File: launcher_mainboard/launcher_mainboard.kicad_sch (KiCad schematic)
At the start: 30 parts, among them J1 USB_B_Micro, J2 Conn_01x06, J3 Conn_01x06, J4 Conn_01x06, J5 Conn_01x06, J6 Conn_01x02, U1 ESP32-S3-MINI-1, U2 TMC2209-LA-T, U3 TMC2209-LA-T, U4 TMC2209-LA-T, U5 TMC2209-LA-T, U6 TLV75801PDRV, U7 R-78E3.3-0.5, U8 D3V3XA4B10LP

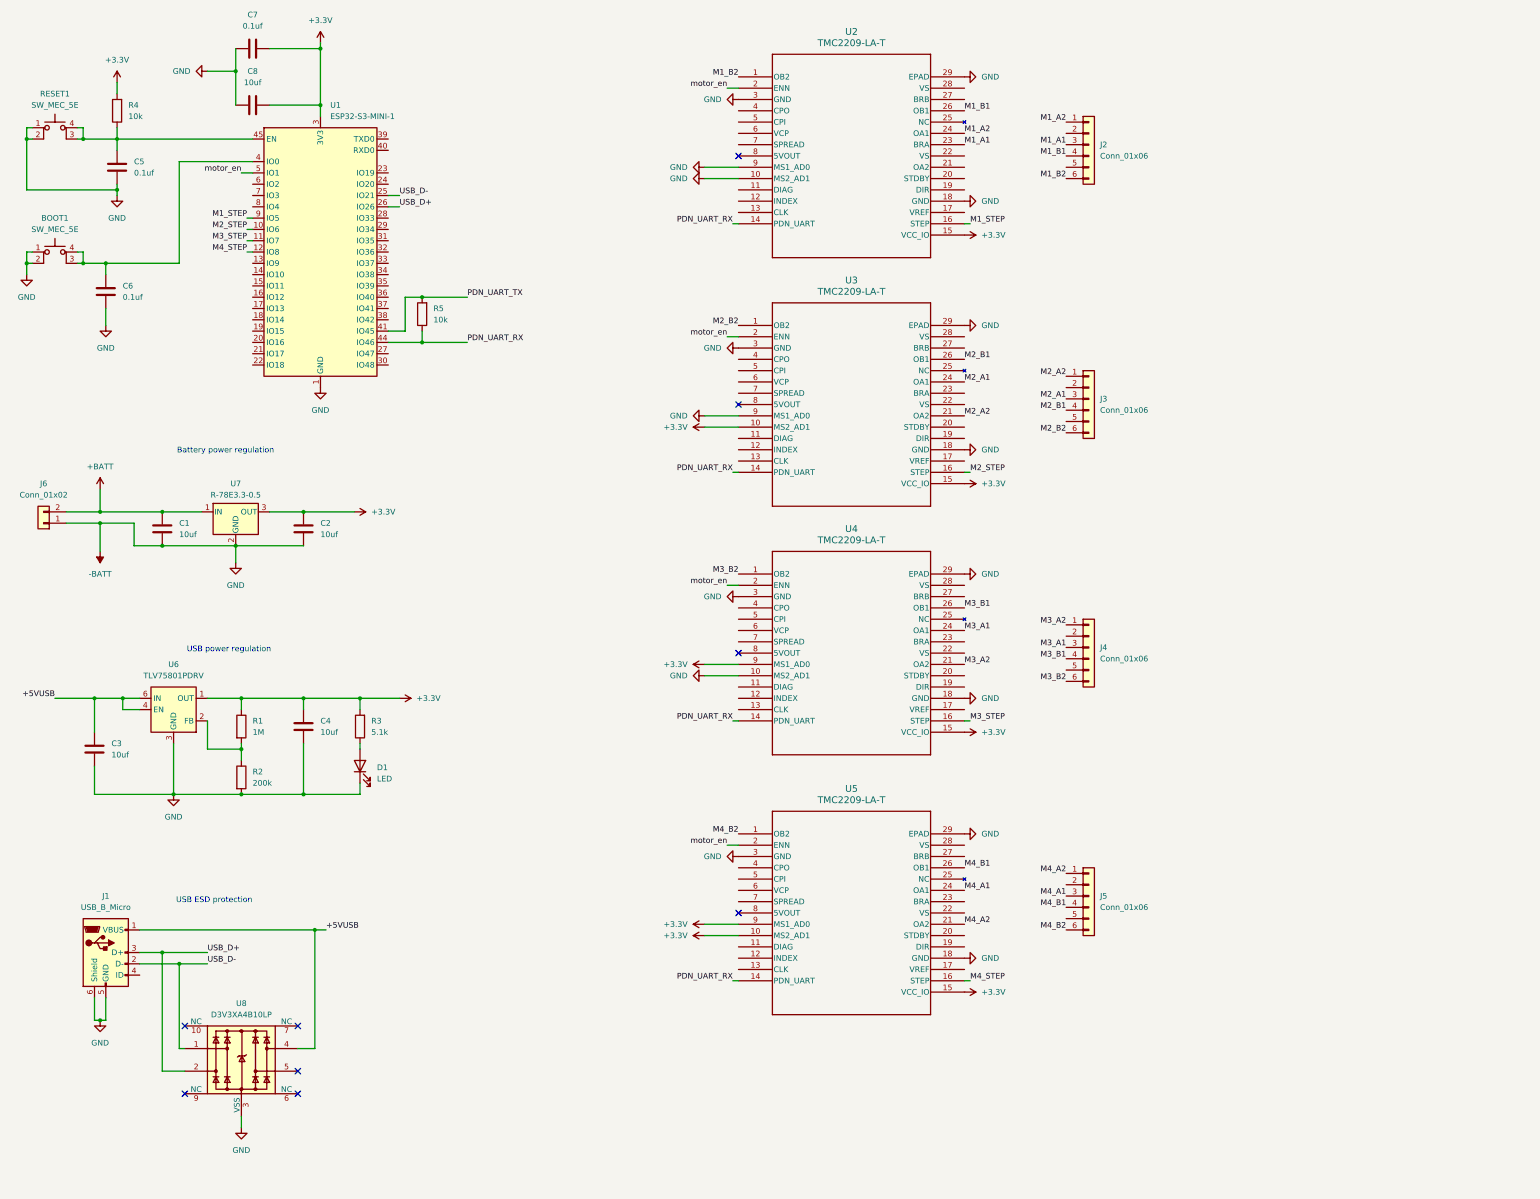
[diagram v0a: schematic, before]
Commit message: battery voltage adc divider
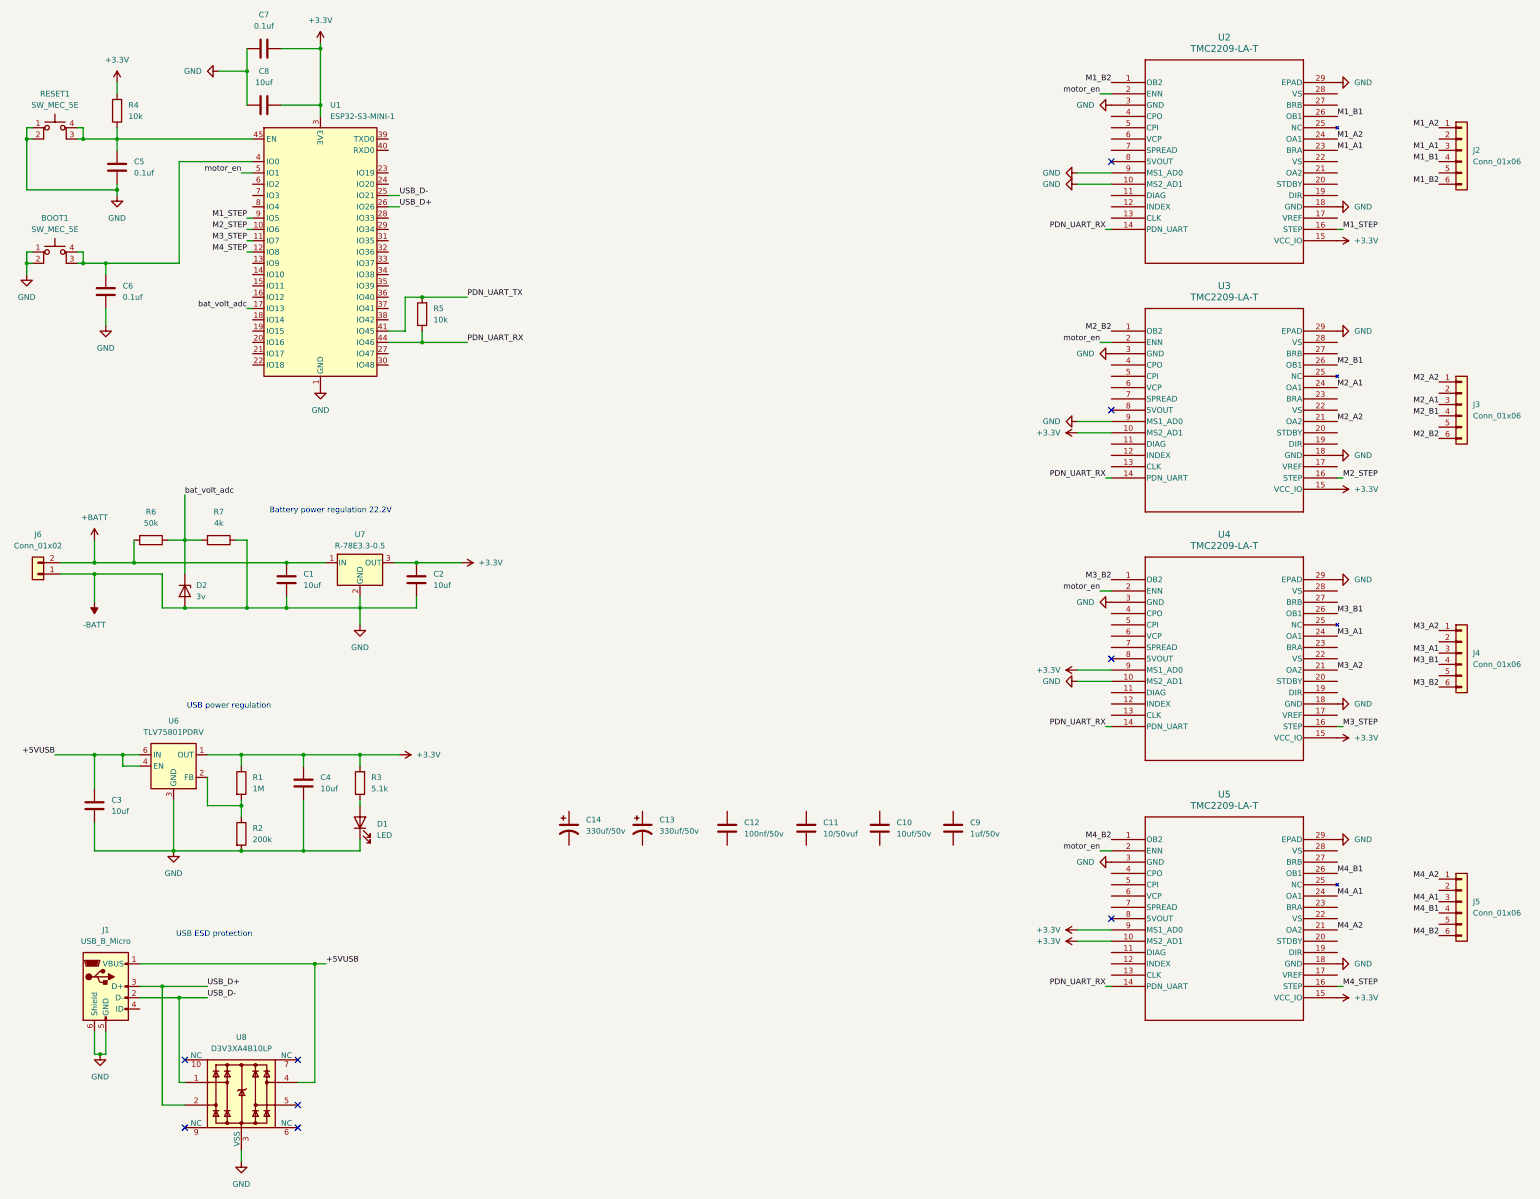
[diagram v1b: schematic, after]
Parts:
- added C10: 10uf/50v, Capacitor_SMD:C_0201_0603Metric, symbol Device:C
- added C11: 10/50vuf, Capacitor_SMD:C_0201_0603Metric, symbol Device:C
- added C12: 100nf/50v, Capacitor_SMD:C_0201_0603Metric, symbol Device:C
- added C13, C14: 330uf/50v, symbol Device:C_Polarized_US
- added C9: 1uf/50v, Capacitor_SMD:C_0201_0603Metric, symbol Device:C
- added D2: 3v, symbol Device:D_Zener
- added R6: 50k, Resistor_SMD:R_0201_0603Metric, symbol Device:R
- added R7: 4k, Resistor_SMD:R_0201_0603Metric, symbol Device:R
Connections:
- net +BATT: now also R6.2
- net -BATT: now also D2.2 (A), R7.1
- net bat_volt_adc: now reaches U1.17 (IO13)
- net bat_volt_adc: now also D2.1 (K), R6.1, R7.2
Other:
- note added: "Battery power regulation 22.2V"
- note removed: "Battery power regulation"
- moved on the sheet: C1, C2, C3, C4, C7, C8, D1, J1, J2, J3, J4, J5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

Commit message: more electricity
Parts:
- removed C10: 10uf/50v, Capacitor_SMD:C_0201_0603Metric, symbol Device:C
- removed C11: 10/50vuf, Capacitor_SMD:C_0201_0603Metric, symbol Device:C
- removed C12: 100nf/50v, Capacitor_SMD:C_0201_0603Metric, symbol Device:C
- removed C13, C14: 330uf/50v, symbol Device:C_Polarized_US
- removed C9: 1uf/50v, Capacitor_SMD:C_0201_0603Metric, symbol Device:C
- added C15, C16: 10uf, Capacitor_SMD:C_0201_0603Metric, symbol Device:C
- added D3: D_Schottky, symbol Device:D_Schottky
- added D4: INDICATOR_LED_1, LED_SMD:LED_PLCC-2_3x2mm_AK, symbol Device:LED
- added D5: INDICATOR_LED_2, LED_SMD:LED_PLCC-2_3x2mm_AK, symbol Device:LED
- added F1: Fuse, symbol Device:Fuse
- added J10: pin headers, Connector_PinHeader_2.54mm:PinHeader_1x14_P2.54mm_Vertical, symbol Connector_Generic:Conn_01x14
- added J7: fan_con, Connector_Molex:Molex_PicoBlade_53047-0210_1x02_P1.25mm_Vertical, symbol Connector_Generic:Conn_01x02
- added J8: ESC_1, Connector_AMASS:AMASS_XT60-F_1x02_P7.20mm_Vertical, symbol Connector_Generic:Conn_01x02
- added J9: ESC_2, Connector_AMASS:AMASS_XT60-F_1x02_P7.20mm_Vertical, symbol Connector_Generic:Conn_01x02
- added Q1: 2N7002H, Package_TO_SOT_SMD:SOT-23, symbol Transistor_FET:2N7002H
- added Q2, Q3: 2N3904, Package_TO_SOT_THT:TO-92_Inline, symbol Transistor_BJT:2N3904
- added Q4, Q5, Q6, Q7: BSS138, Package_TO_SOT_SMD:SOT-23, symbol Transistor_FET:BSS138
- added R10, R12: 200, Resistor_SMD:R_0201_0603Metric, symbol Device:R
- added R11, R13: 20k, Resistor_SMD:R_0201_0603Metric, symbol Device:R
- added R14, R15, R16, R17, R18, R19, R20, R21: 10k, Resistor_SMD:R_0201_0603Metric, symbol Device:R
- added R22, R24, R26, R28: 50k, Resistor_SMD:R_0201_0603Metric, symbol Device:R
- added R23, R25, R27, R29: 75k, Resistor_SMD:R_0201_0603Metric, symbol Device:R
- added R8, R9: ?, Resistor_SMD:R_0201_0603Metric, symbol Device:R
- added U9: R-78E5.0-0.5, Converter_DCDC:Converter_DCDC_RECOM_R-78E-0.5_THT, symbol Regulator_Switching:R-78E5.0-0.5
- D1: value LED -> POWER_LED
- J6: value Conn_01x02 -> bat_con
- R3: value 5.1k -> 200
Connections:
- net +3.3V: now also Q4.1 (G), Q5.1 (G), Q6.1 (G), Q7.1 (G), R10.1, R12.1, R14.2, R16.2, R18.2, R20.2
- net +BATT: now also C15.1, D3.1 (K), F1.2, J7.1 (Pin_1), J8.2 (Pin_2), J9.2 (Pin_2), U9.1 (IN); no longer J6.2 (Pin_2)
- net -BATT: now also C15.2, C16.2, J8.1 (Pin_1), J9.1 (Pin_1), Q1.2 (S), Q2.1 (E), Q3.1 (E), R23.1, R25.1, R27.1, R29.1, R8.1, U9.2 (GND)
- net M1_STEP: no longer U1.9 (IO5)
- net M2_STEP: no longer U1.10 (IO6)
- net M3_STEP: no longer U1.11 (IO7)
- net M4_STEP: no longer U1.12 (IO8)
- net USB_D+: no longer U1.26 (IO26)
- net USB_D-: no longer U1.25 (IO21)
- net bat_volt_adc: no longer U1.17 (IO13)
- net M3_DIR: now reaches U4.19 (DIR)
- net M2_DIR: now reaches U3.19 (DIR)
- net M1_DIR: now reaches U2.19 (DIR)
- net M4_DIR: now reaches U5.19 (DIR)
- net ind_LED_1: now reaches U1.14 (IO10)
- net ind_LED_1: now also R11.1
- net ind_LED_2: now reaches U1.15 (IO11)
- net ind_LED_2: now also R13.1
- net +5VUSB renamed +5V
- net +5V: now also C16.1, R15.2, R17.2, R19.2, R21.2, U9.3 (OUT)
- new net: D4.1 (K), Q2.3 (C)
- new net: D4.2 (A), R10.2
- new net: Q3.2 (B), R13.2
- new net: D5.1 (K), Q3.3 (C)
- new net: D5.2 (A), R12.2
- new net: Q1.1 (G), R8.2, R9.1
- new net: Q2.2 (B), R11.2
- new net: F1.1, J6.2 (Pin_2)
- new net: D3.2 (A), J7.2 (Pin_2), Q1.3 (D)
- new net HV1: Q4.3 (D), R15.1
- new net HV2: Q5.3 (D), R17.1
- new net HV3: Q6.3 (D), R19.1
- new net HV4: Q7.3 (D), R21.1
- new net HV_SIGNAL_1: R22.2
- new net HV_SIGNAL_2: R24.2
- new net HV_SIGNAL_3: R26.2
- new net HV_SIGNAL_4: R28.2
- new net LV1: Q4.2 (S), R14.1
- new net LV2: Q5.2 (S), R16.1
- new net LV3: Q6.2 (S), R18.1
- new net LV4: Q7.2 (S), R20.1
- new net LV_SIGNAL_1: R22.1, R23.2
- new net LV_SIGNAL_2: R24.1, R25.2
- new net LV_SIGNAL_3: R26.1, R27.2
- new net LV_SIGNAL_4: R28.1, R29.2
- new net fan_ctrl: R9.2
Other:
- note added: "3.3V rail"
- note added: "5.0V rail"
- note added: "Battery power input 22.2V"
- note added: "ESC power distribution"
- note added: "Fan driver"
- note added: "Indicator LED drivers"
- note added: "Level shifted bi-directional GPIO"
- note added: "Level shifted signal GPIO"
- note removed: "Battery power regulation 22.2V"
- moved on the sheet: C1, C2, D2, J2, J3, J4, J5, J6, R6, R7, U2, U3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

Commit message: uhhh
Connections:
- net +5V: no longer C3.1, J1.1 (VBUS), U6.4 (EN), U6.6 (IN), U8.4
- new net +5VUSB: C3.1, J1.1 (VBUS), U6.4 (EN), U6.6 (IN), U8.4
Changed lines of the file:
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@@
 		)
 	)
+	(label "+5VUSB"
+		(at 86.36 229.87 0)
+		(fields_autoplaced yes)
+		(effects
+			(font
+				(size 1.27 1.27)
+			)
+			(justify left bottom)
+		)
+	)
 	(label "HV3"
 		(at 139.7 198.12 180)
@@
 		)
 	)
+	(label "+5VUSB"
+		(at 25.4 182.88 180)
+		(fields_autoplaced yes)
+		(effects
+			(font
+				(size 1.27 1.27)
+			)
+			(justify right bottom)
+		)
+	)
 	(label "LV_SIGNAL_3"
 		(at 68.58 59.69 180)
@@
 	)
 	(symbol
-		(lib_id "power:+5V")
-		(at 86.36 229.87 270)
-		(unit 1)
-		(exclude_from_sim no)
-		(in_bom yes)
-		(on_board yes)
-		(dnp no)
-		(fields_autoplaced yes)
-		(property "Reference" "#PWR055"
-			(at 82.55 229.87 0)
-			(effects
-				(font
-					(size 1.27 1.27)
-				)
-				(hide yes)
-			)
-		)
-		(property "Value" "+5V"
-			(at 90.17 229.8699 90)
-			(effects
-				(font
-					(size 1.27 1.27)
-				)
-				(justify left)
-			)
-		)
-		(property "Footprint" ""
-			(at 86.36 229.87 0)
-			(effects
-				(font
-					(size 1.27 1.27)
-				)
-				(hide yes)
-			)
-		)
-		(property "Datasheet" ""
-			(at 86.36 229.87 0)
-			(effects
-				(font
-					(size 1.27 1.27)
-				)
-				(hide yes)
-			)
-		)
-		(property "Description" "Power symbol creates a global label with name \"+5V\""
-			(at 86.36 229.87 0)
-			(effects
-				(font
-					(size 1.27 1.27)
-				)
-				(hide yes)
-			)
-		)
-		(pin "1"
-		)
-		(instances
-			(project "launcher_mainboard"
-				(path "/c708c50f-809b-4d12-a774-1744101f70a6"
-					(reference "#PWR055")
-					(unit 1)
-				)
-			)
-		)
-	)
-	(symbol
 		(lib_id "Connector_Generic:Conn_01x02")
 		(at 168.91 31.75 0)
@@
 					(unit 1)
 				)
-			)
-		)
-	)
-	(symbol
-		(lib_id "power:+5V")
-		(at 25.4 182.88 90)
-		(unit 1)
-		(exclude_from_sim no)
-		(in_bom yes)
-		(on_board yes)
-		(dnp no)
-		(fields_autoplaced yes)
-		(property "Reference" "#PWR056"
-			(at 29.21 182.88 0)
-			(effects
-				(font
-					(size 1.27 1.27)
-				)
-				(hide yes)
-			)
-		)
-		(property "Value" "+5V"
-			(at 21.59 182.8799 90)
-			(effects
-				(font
-					(size 1.27 1.27)
-				)
-				(justify left)
-			)
-		)
-		(property "Footprint" ""
-			(at 25.4 182.88 0)
-			(effects
-				(font
-					(size 1.27 1.27)
-				)
-				(hide yes)
-			)
-		)
-		(property "Datasheet" ""
-			(at 25.4 182.88 0)
-			(effects
-				(font
-					(size 1.27 1.27)
-				)
-				(hide yes)
-			)
-		)
-		(property "Description" "Power symbol creates a global label with name \"+5V\""
-			(at 25.4 182.88 0)
-			(effects
-				(font
-					(size 1.27 1.27)
-				)
-				(hide yes)
-			)
-		)
-		(pin "1"
-		)
-		(instances
-			(project "launcher_mainboard"
-				(path "/c708c50f-809b-4d12-a774-1744101f70a6"
-					(reference "#PWR056")
-					(unit 1)
-				)

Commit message: ellectt elelecitfy
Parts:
- added C10, C11, C12, C9: 220uf, Capacitor_SMD:CP_Elec_3x5.3, symbol Device:C_Polarized_US
- added D6: D_Schottky, Diode_SMD:D_0201_0603Metric, symbol Device:D_Schottky
- added Q8: PMOS, Package_DFN_QFN:DFN-6-1EP_2x1.6mm_P0.5mm_EP1.15x1.3mm, symbol Simulation_SPICE:PMOS
- added U10: MAX40200AUK, Package_TO_SOT_SMD:SOT-23-5, symbol Analog_Switch:MAX40200AUK
- D2, D3: footprint (none) -> Diode_SMD:D_0201_0603Metric
- F1: footprint (none) -> Fuse:FuseHolder_Blade_ATO_Littelfuse_FLR_178.6165
- U2: footprint TMC2209-LA-T:QFN28_5X5_3X8_EPAD_TRI -> CustomFootprints:TCM2209_Module
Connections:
- net +3.3V: now also D6.1 (K), U10.5 (OUT); no longer C2.1, C4.1, R1.1, R3.2, U6.1 (OUT), U7.3 (OUT)
- net +BATT: now also U2.22 (VS), U2.28 (VS), U3.22 (VS), U3.28 (VS), U4.22 (VS), U4.28 (VS), U5.22 (VS), U5.28 (VS), C10.1, C11.1, C12.1, C9.1
- net -BATT: now also C10.2, C11.2, C12.2, C9.2, U10.2 (GND)
- net M1_A1: now also U2.24 (OA1); no longer U2.23 (BRA)
- net M1_A2: now also U2.21 (OA2); no longer U2.24 (OA1)
- new net: Q8.1 (D), U10.3 (EN)
- new net +3.3VBatt: C2.1, Q8.3 (S), U10.1 (VDD), U7.3 (OUT)
- new net 3.5VUSB: C4.1, D6.2 (A), Q8.2 (G), R1.1, R3.2, U6.1 (OUT)
- no-connect marks 9 -> 53
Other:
- moved on the sheet: C1, C15, C16, C2, D3, J10, J2, J3, J4, J5, J7, J8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

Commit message: power selector, moved some files
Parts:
- removed D6: D_Schottky, Diode_SMD:D_0201_0603Metric, symbol Device:D_Schottky
- removed Q8: PMOS, Package_DFN_QFN:DFN-6-1EP_2x1.6mm_P0.5mm_EP1.15x1.3mm, symbol Simulation_SPICE:PMOS
- removed U10: MAX40200AUK, Package_TO_SOT_SMD:SOT-23-5, symbol Analog_Switch:MAX40200AUK
- added SW1: POWER_SWITCH, symbol Switch:SW_DIP_x01
- added U12: LM66200DRLR, LM66200:SOT-5X3_DRL_TEX, symbol LM66200:LM66200DRLR
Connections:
- net +3.3V: now also U12.2 (VOUT), U12.7 (VOUT)
- net +3.3VBatt: now also U12.3 (VIN1)
- net -BATT: now also U12.1 (GND), U12.4 (ON), U12.5 (GND)
- net at J6.2 (Pin_2): now also SW1.1; no longer F1.1
- net 3.5VUSB renamed 3.3VUSB
- net 3.3VUSB: now also U12.6 (VIN2)
- new net: F1.1, SW1.2
- no-connect marks 53 -> 54
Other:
- note added: "3.3V power source selection"
- moved on the sheet: J6
